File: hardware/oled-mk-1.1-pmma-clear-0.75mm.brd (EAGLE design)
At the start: 72 x 34 mm, 0 parts

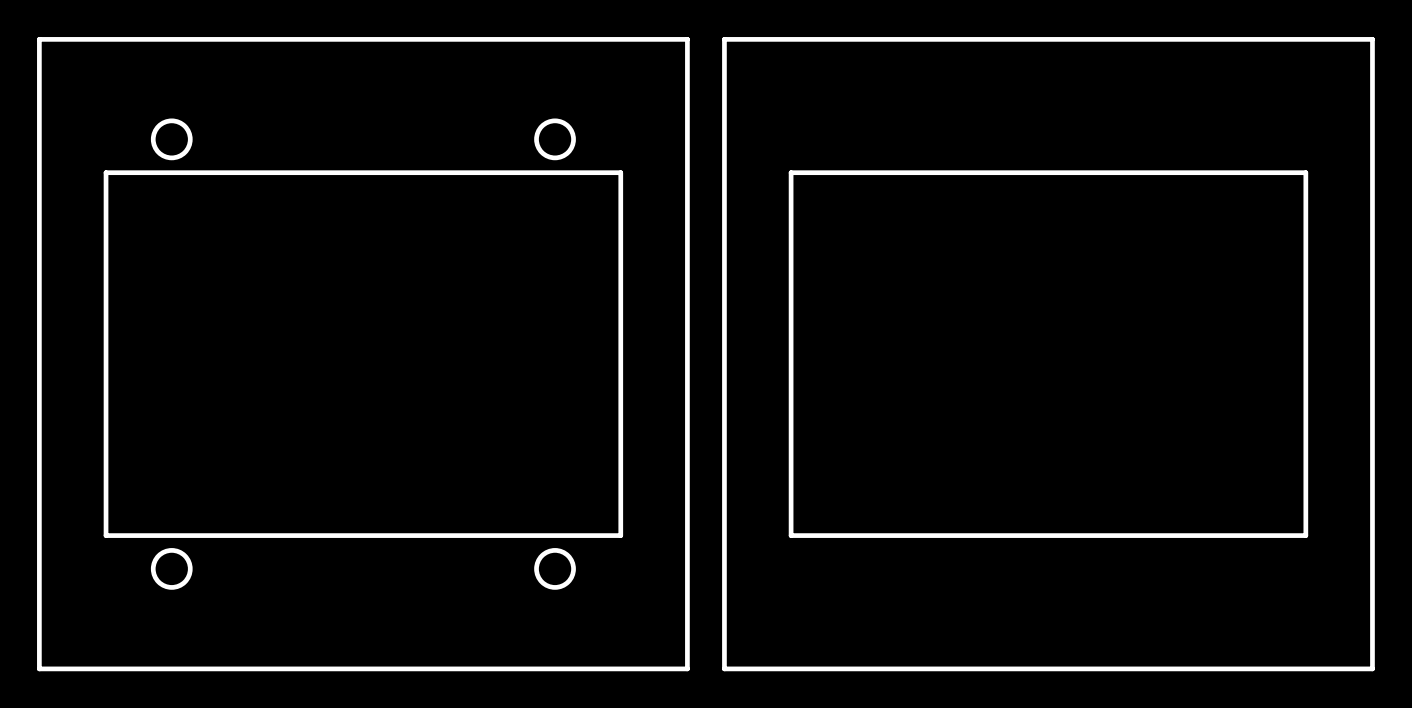
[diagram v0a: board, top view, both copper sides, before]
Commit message: layout for laser cutting
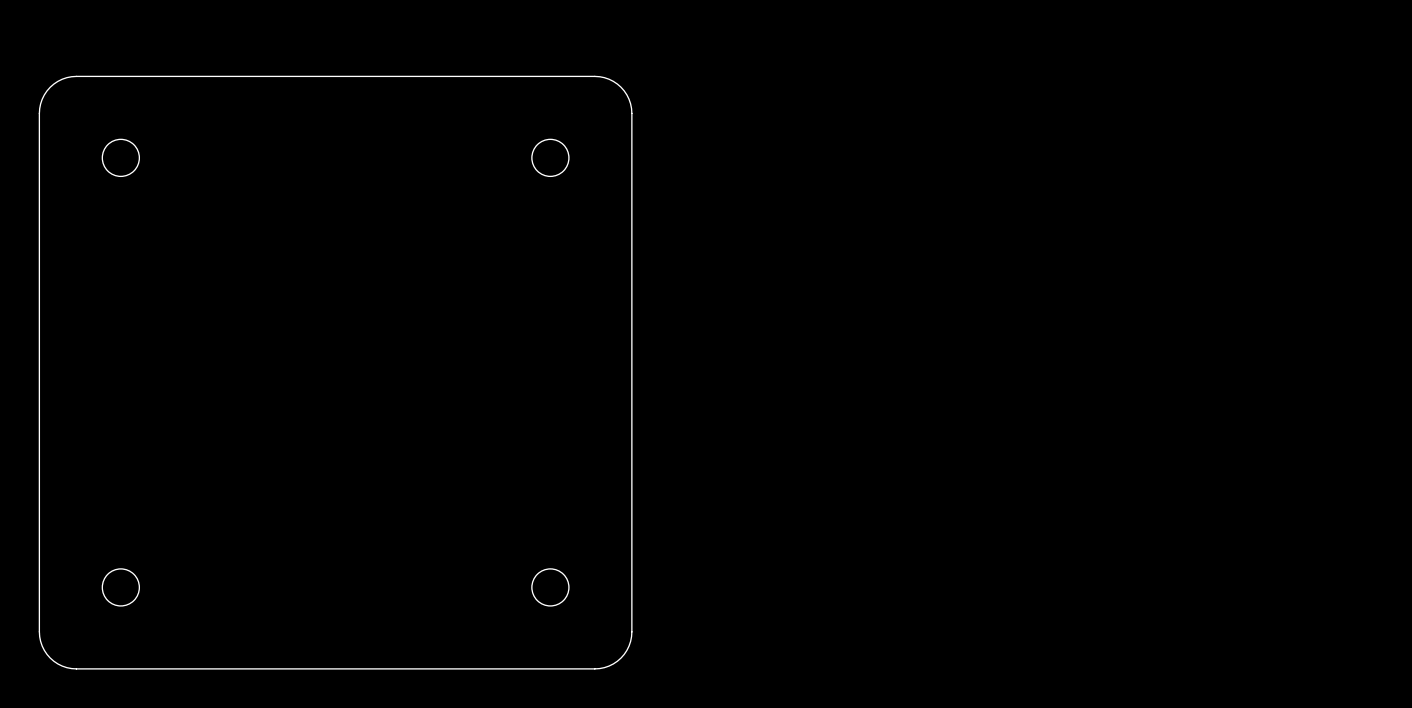
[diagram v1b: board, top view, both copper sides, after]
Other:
- board size 72 x 34 mm -> 32 x 32 mm
- board text added: "1.00 in calibration sq"
- board text added: "Layer 1 Clear Acrylic (0.75mm)"
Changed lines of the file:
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@@
 <layer number="29" name="tStop" color="7" fill="3" visible="yes" active="yes"/>
 <layer number="30" name="bStop" color="7" fill="6" visible="yes" active="yes"/>
-<layer number="31" name="tCream" color="7" fill="4" visible="no" active="yes"/>
-<layer number="32" name="bCream" color="7" fill="5" visible="no" active="yes"/>
-<layer number="33" name="tFinish" color="6" fill="3" visible="no" active="yes"/>
-<layer number="34" name="bFinish" color="6" fill="6" visible="no" active="yes"/>
-<layer number="35" name="tGlue" color="7" fill="4" visible="no" active="yes"/>
-<layer number="36" name="bGlue" color="7" fill="5" visible="no" active="yes"/>
-<layer number="37" name="tTest" color="7" fill="1" visible="no" active="yes"/>
-<layer number="38" name="bTest" color="7" fill="1" visible="no" active="yes"/>
+<layer number="31" name="tCream" color="7" fill="4" visible="yes" active="yes"/>
+<layer number="32" name="bCream" color="7" fill="5" visible="yes" active="yes"/>
+<layer number="33" name="tFinish" color="6" fill="3" visible="yes" active="yes"/>
+<layer number="34" name="bFinish" color="6" fill="6" visible="yes" active="yes"/>
+<layer number="35" name="tGlue" color="7" fill="4" visible="yes" active="yes"/>
+<layer number="36" name="bGlue" color="7" fill="5" visible="yes" active="yes"/>
+<layer number="37" name="tTest" color="7" fill="1" visible="yes" active="yes"/>
+<layer number="38" name="bTest" color="7" fill="1" visible="yes" active="yes"/>
 <layer number="39" name="tKeepout" color="4" fill="11" visible="yes" active="yes"/>
 <layer number="40" name="bKeepout" color="1" fill="11" visible="yes" active="yes"/>
@@
 <layer number="42" name="bRestrict" color="1" fill="10" visible="yes" active="yes"/>
 <layer number="43" name="vRestrict" color="2" fill="10" visible="yes" active="yes"/>
-<layer number="44" name="Drills" color="7" fill="1" visible="no" active="yes"/>
+<layer number="44" name="Drills" color="7" fill="1" visible="yes" active="yes"/>
 <layer number="45" name="Holes" color="7" fill="1" visible="yes" active="yes"/>
-<layer number="46" name="Milling" color="3" fill="1" visible="no" active="yes"/>
+<layer number="46" name="Milling" color="3" fill="1" visible="yes" active="yes"/>
 <layer number="47" name="Measures" color="7" fill="1" visible="yes" active="yes"/>
 <layer number="48" name="Document" color="7" fill="1" visible="yes" active="yes"/>
@@
 <board>
 <plain>
-<wire x1="0" y1="34" x2="35" y2="34" width="0.254" layer="20"/>
-<wire x1="35" y1="34" x2="35" y2="0" width="0.254" layer="20"/>
-<wire x1="35" y1="0" x2="0" y2="0" width="0.254" layer="20"/>
-<wire x1="0" y1="0" x2="0" y2="34" width="0.254" layer="20"/>
-<wire x1="3.85" y1="30.65" x2="3.85" y2="3.35" width="0.1524" layer="51"/>
-<wire x1="3.85" y1="3.35" x2="31.15" y2="3.35" width="0.1524" layer="51"/>
-<wire x1="31.15" y1="3.35" x2="31.15" y2="30.65" width="0.1524" layer="51"/>
-<wire x1="31.15" y1="30.65" x2="3.85" y2="30.65" width="0.1524" layer="51"/>
-<wire x1="3.85" y1="7.5" x2="31.15" y2="7.5" width="0.1524" layer="52"/>
-<wire x1="3.85" y1="26.5" x2="31.15" y2="26.5" width="0.1524" layer="52"/>
-<wire x1="3.85" y1="7.5" x2="3.85" y2="26.5" width="0.1524" layer="52"/>
-<wire x1="31.15" y1="26.5" x2="31.15" y2="7.5" width="0.1524" layer="52"/>
-<wire x1="3.6" y1="7.2" x2="3.6" y2="26.8" width="0.254" layer="20"/>
-<wire x1="31.4" y1="7.2" x2="31.4" y2="26.8" width="0.254" layer="20"/>
-<wire x1="31.4" y1="26.8" x2="3.6" y2="26.8" width="0.254" layer="20"/>
-<wire x1="31.4" y1="7.2" x2="3.6" y2="7.2" width="0.254" layer="20"/>
-<circle x="7.15" y="28.6" radius="1" width="0.254" layer="20"/>
-<circle x="27.85" y="28.6" radius="1" width="0.254" layer="20"/>
-<circle x="27.85" y="5.4" radius="1" width="0.254" layer="20"/>
-<circle x="7.15" y="5.4" radius="1" width="0.254" layer="20"/>
-<wire x1="37" y1="34" x2="72" y2="34" width="0.254" layer="20"/>
-<wire x1="72" y1="34" x2="72" y2="0" width="0.254" layer="20"/>
-<wire x1="72" y1="0" x2="37" y2="0" width="0.254" layer="20"/>
-<wire x1="37" y1="0" x2="37" y2="34" width="0.254" layer="20"/>
-<wire x1="40.6" y1="7.2" x2="40.6" y2="26.8" width="0.254" layer="20"/>
-<wire x1="68.4" y1="7.2" x2="68.4" y2="26.8" width="0.254" layer="20"/>
-<wire x1="68.4" y1="26.8" x2="40.6" y2="26.8" width="0.254" layer="20"/>
-<wire x1="68.4" y1="7.2" x2="40.6" y2="7.2" width="0.254" layer="20"/>
-<wire x1="40.85" y1="30.65" x2="40.85" y2="3.35" width="0.1524" layer="51"/>
-<wire x1="40.85" y1="3.35" x2="68.15" y2="3.35" width="0.1524" layer="51"/>
-<wire x1="68.15" y1="3.35" x2="68.15" y2="30.65" width="0.1524" layer="51"/>
-<wire x1="68.15" y1="30.65" x2="40.85" y2="30.65" width="0.1524" layer="51"/>
+<wire x1="50.8" y1="25.4" x2="50.8" y2="0" width="0.1524" layer="47"/>
+<wire x1="50.8" y1="0" x2="76.2" y2="0" width="0.1524" layer="47"/>
+<wire x1="76.2" y1="0" x2="76.2" y2="25.4" width="0.1524" layer="47"/>
+<wire x1="76.2" y1="25.4" x2="50.8" y2="25.4" width="0.1524" layer="47"/>
+<text x="64" y="12.7" size="1.27" layer="47" font="vector" ratio="12" align="center">1.00 in
+calibration sq</text>
+<text x="16" y="35" size="1.27" layer="48" font="vector" ratio="12" align="center">Layer 1
+Clear Acrylic (0.75mm)</text>
+<wire x1="30" y1="0" x2="2" y2="0" width="0.05" layer="20"/>
+<wire x1="2" y1="0" x2="0" y2="2" width="0.05" layer="20" curve="-90"/>
+<wire x1="0" y1="2" x2="0" y2="30" width="0.05" layer="20"/>
+<wire x1="0" y1="30" x2="2" y2="32" width="0.05" layer="20" curve="-90"/>
+<wire x1="2" y1="32" x2="30" y2="32" width="0.05" layer="20"/>
+<wire x1="30" y1="32" x2="32" y2="30" width="0.05" layer="20" curve="-90"/>
+<wire x1="32" y1="30" x2="32" y2="2" width="0.05" layer="20"/>
+<wire x1="32" y1="2" x2="30" y2="0" width="0.05" layer="20" curve="-90"/>
+<circle x="4.4" y="27.6" radius="1" width="0.05" layer="20"/>
+<circle x="27.6" y="27.6" radius="1" width="0.05" layer="20"/>
+<circle x="27.6" y="4.4" radius="1" width="0.05" layer="20"/>
+<circle x="4.4" y="4.4" radius="1" width="0.05" layer="20"/>
 </plain>
 <attributes>
@@
 </board>
 </drawing>
+<compatibility>
+<note version="6.3" minversion="6.2.2" severity="warning">
+Since Version 6.2.2 text objects can contain more than one line,
+which will not be processed correctly with this version.
+</note>
+</compatibility>
 </eagle>
